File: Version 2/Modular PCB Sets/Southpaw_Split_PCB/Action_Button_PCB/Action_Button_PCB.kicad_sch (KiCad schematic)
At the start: 26 parts, among them J2 Conn_01x07_Socket, U1 Pico, X1 SW_SPST, Y1 SW_SPST

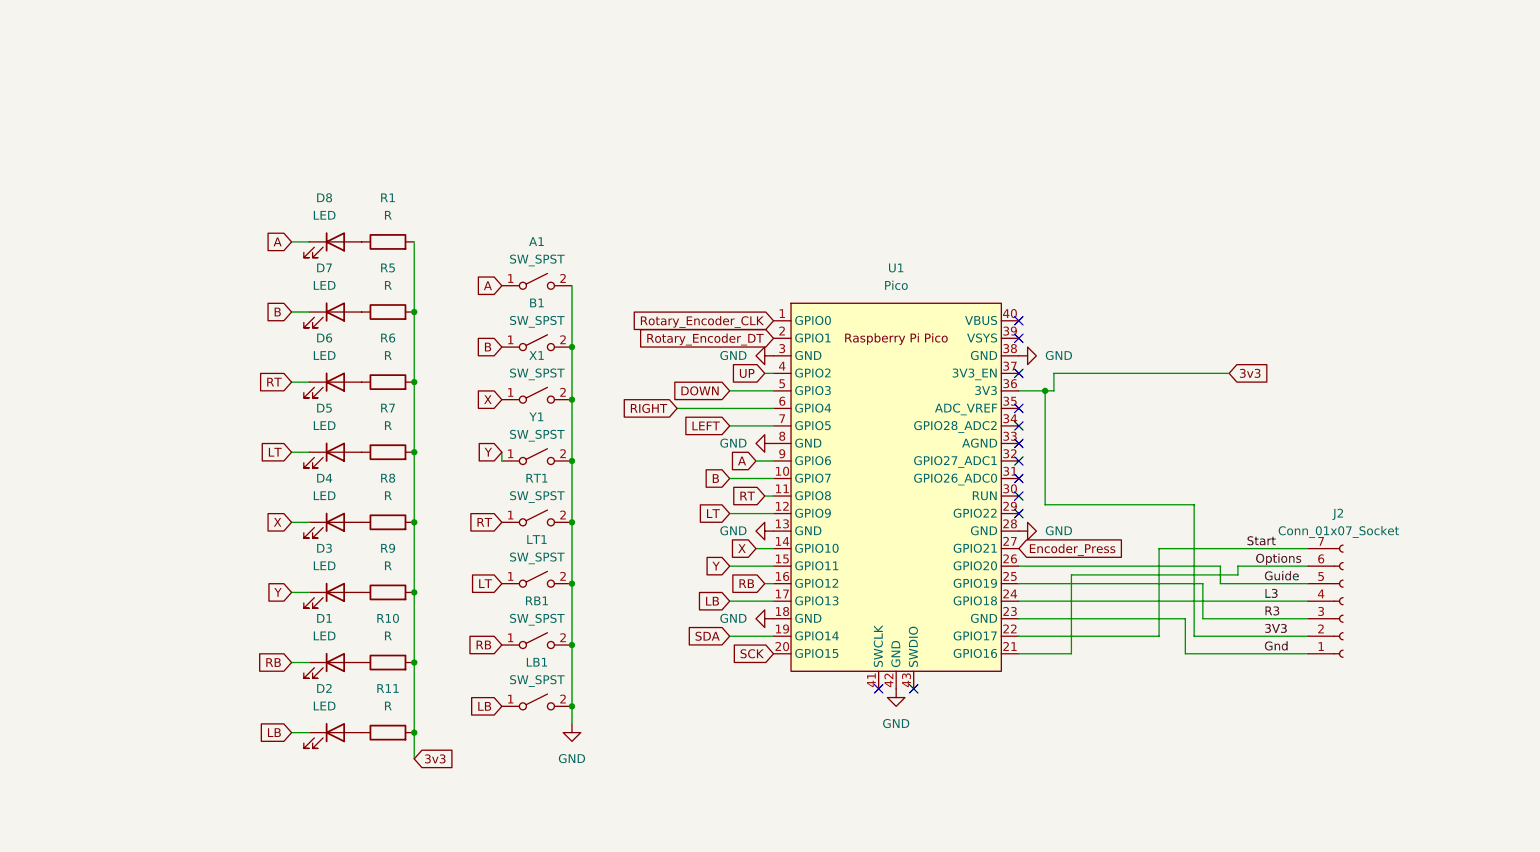
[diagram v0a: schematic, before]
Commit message: rework for schematic structure to accomodate new pico symbol and jst connectors
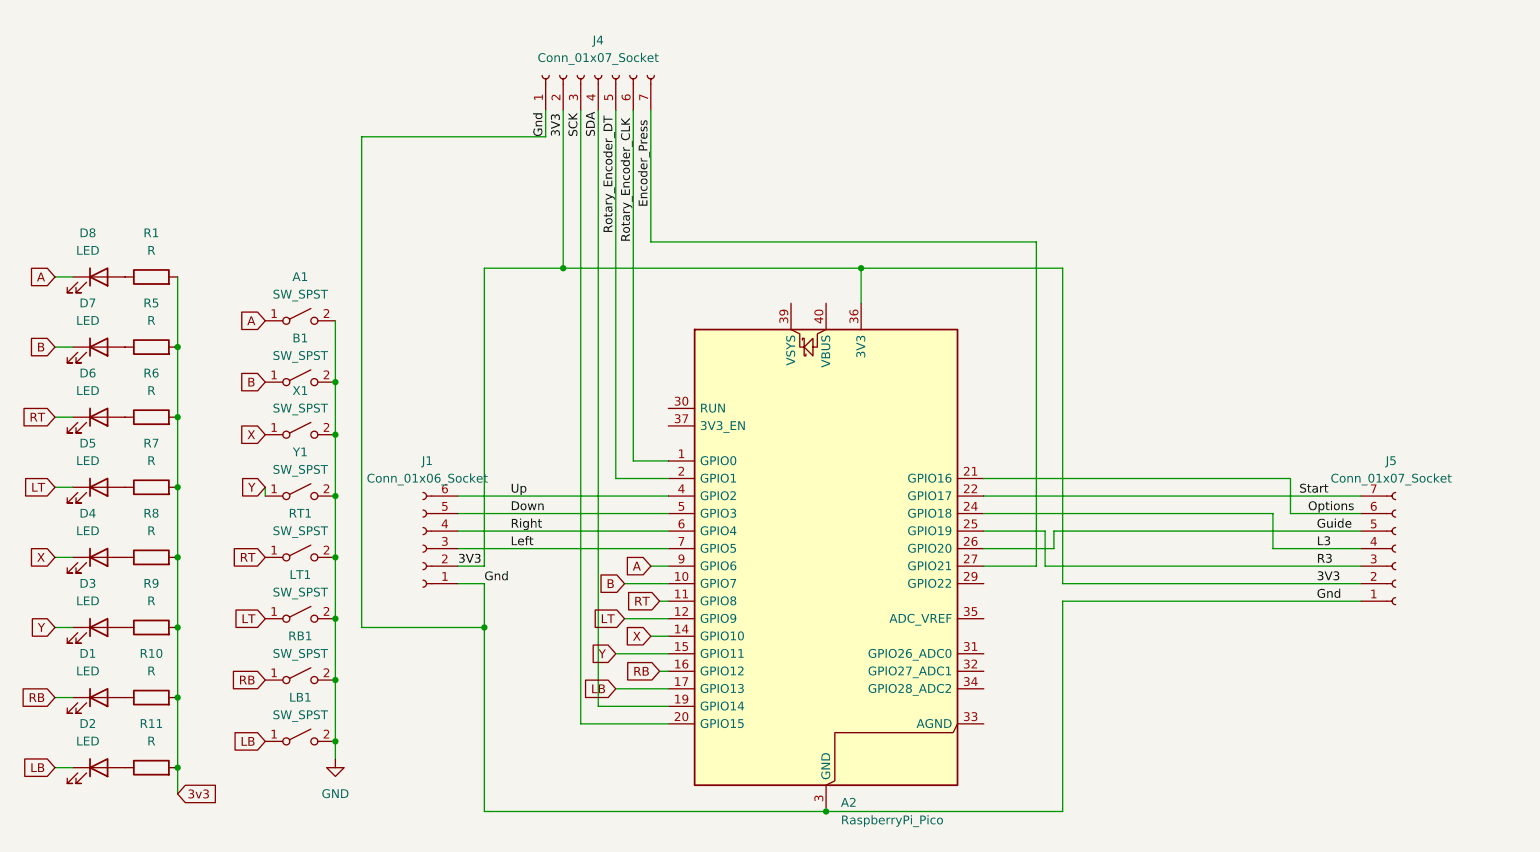
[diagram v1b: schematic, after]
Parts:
- removed J2: Conn_01x07_Socket, Connector_JST:JST_PH_B7B-PH-K_1x07_P2.00mm_Vertical, symbol Connector:Conn_01x07_Socket
- removed U1: Pico, PICO:RPi_Pico_SMD_TH, symbol pico:Pico
- added A2: RaspberryPi_Pico, Module:RaspberryPi_Pico_Common_Unspecified, symbol MCU_Module:RaspberryPi_Pico
- added J1: Conn_01x06_Socket, Connector_JST:JST_PH_B6B-PH-K_1x06_P2.00mm_Vertical, symbol Connector:Conn_01x06_Socket
- added J4, J5: Conn_01x07_Socket, Connector_JST:JST_PH_B7B-PH-K_1x07_P2.00mm_Vertical, symbol Connector:Conn_01x07_Socket
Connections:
- net A: now also A2.9 (GPIO6)
- net B: now also A2.10 (GPIO7)
- net Encoder_Press: now also A2.27 (GPIO21), J4.7 (Pin_7)
- net Gnd: now also A2.13 (GND), A2.18 (GND), A2.23 (GND), A2.28 (GND), A2.3 (GND), A2.38 (GND), A2.8 (GND), J1.1 (Pin_1), J4.1 (Pin_1), J5.1 (Pin_1)
- net Guide: now also A2.26 (GPIO20), J5.5 (Pin_5)
- net L3: now also A2.24 (GPIO18), J5.4 (Pin_4)
- net LB: now also A2.17 (GPIO13)
- net LT: now also A2.12 (GPIO9)
- net Options: now also A2.21 (GPIO16), J5.6 (Pin_6)
- net R3: now also A2.25 (GPIO19), J5.3 (Pin_3)
- net RB: now also A2.16 (GPIO12)
- net RT: now also A2.11 (GPIO8)
- net Rotary_Encoder_CLK: now also A2.1 (GPIO0), J4.6 (Pin_6)
- net Rotary_Encoder_DT: now also A2.2 (GPIO1), J4.5 (Pin_5)
- net SCK: now also A2.20 (GPIO15), J4.3 (Pin_3)
- net SDA: now also A2.19 (GPIO14), J4.4 (Pin_4)
- net Start: now also A2.22 (GPIO17), J5.7 (Pin_7)
- net X: now also A2.14 (GPIO10)
- net Y: now also A2.15 (GPIO11)
- new net 3V3: A2.36 (3V3), J1.2 (Pin_2), J4.2 (Pin_2), J5.2 (Pin_2)
- new net Down: A2.5 (GPIO3), J1.5 (Pin_5)
- new net Left: A2.7 (GPIO5), J1.3 (Pin_3)
- new net Right: A2.6 (GPIO4), J1.4 (Pin_4)
- new net Up: A2.4 (GPIO2), J1.6 (Pin_6)
- no-connect marks 12 -> 0
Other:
- moved on the sheet: A1, B1, D1, D2, D3, D4, D5, D6, D7, D8, LB1, LT1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

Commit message: created footprints for all lockout and oled display
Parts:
- renumbered D8 to D10, D7 to D11, D6 to D12, D5 to D13, D4 to D14, D3 to D15, D1 to D16, D2 to D17, J1 to J4, J4 to J5, J5 to J6, R1 to R11, R5 to R12, R6 to R13, R7 to R14, R8 to R15, R9 to R16, R10 to R17, R11 to R18

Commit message: general part layout
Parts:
- renumbered R11 to R10, R12 to R11, R13 to R12, R14 to R13, R15 to R14, R16 to R15, R17 to R16, R18 to R17
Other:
- moved on the sheet: A1, A2, B1, D10, D11, D12, D13, D14, D15, D16, D17, J4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

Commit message: First attempt to use solidworks sketches to align parts in kicad
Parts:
- renumbered D10 to D1, D11 to D2, D12 to D3, D13 to D4, D14 to D5, D15 to D6, D16 to D7, D17 to D8, J4 to J1, J5 to J2, J6 to J3, R10 to R1, R11 to R2, R12 to R3, R13 to R4, R14 to R5, R15 to R6, R16 to R7, R17 to R8
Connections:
- net 3V3 is gone; now on net 3v3: A2.36 (3V3), J1.2 (Pin_2), J2.2 (Pin_2), J3.2 (Pin_2)
- net Gnd is gone; now on net GND: A2.13 (GND), A2.18 (GND), A2.23 (GND), A2.28 (GND), A2.3 (GND), A2.38 (GND), A2.8 (GND), J1.1 (Pin_1), J2.1 (Pin_1), J3.1 (Pin_1)
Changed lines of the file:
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@@
+		)
+	)
+	(global_label "3v3"
+		(shape input)
+		(at 208.28 60.96 0)
+		(fields_autoplaced yes)
+		(effects
+			(font
+				(size 1.27 1.27)
+			)
+			(justify left)
+		)
+		(property "Intersheetrefs" "${INTERSHEET_REFS}"
+			(at 214.6518 60.96 0)
+			(effects
+				(font
+					(size 1.27 1.27)
+				)
+				(justify left)
+				(hide yes)
+			)
 		)
 	)
@@
 		(dnp no)
 		(fields_autoplaced yes)
-		(property "Reference" "J4"
+		(property "Reference" "J1"
 			(at 116.205 88.9 0)
 			(effects
@@
 		(dnp no)
 		(fields_autoplaced yes)
-		(property "Reference" "R14"
+		(property "Reference" "R5"
 			(at 76.2 96.52 90)
 			(effects
@@
 		(dnp no)
 		(fields_autoplaced yes)
-		(property "Reference" "R15"
+		(property "Reference" "R6"
 			(at 76.2 106.68 90)
 			(effects
@@
 		(dnp no)
 		(fields_autoplaced yes)
-		(property "Reference" "D15"
+		(property "Reference" "D6"
 			(at 66.9925 106.68 0)
 			(effects
@@
 		(dnp no)
 		(fields_autoplaced yes)
-		(property "Reference" "D12"
+		(property "Reference" "D3"
 			(at 66.9925 76.2 0)
 			(effects
@@
 		(dnp no)
 		(fields_autoplaced yes)
-		(property "Reference" "R13"
+		(property "Reference" "R4"
 			(at 76.2 86.36 90)
 			(effects
@@
 		(dnp no)
 		(fields_autoplaced yes)
-		(property "Reference" "D16"
+		(property "Reference" "D7"
 			(at 66.9925 116.84 0)
 			(effects
@@
 	)
 	(symbol
+		(lib_id "power:GND")
+		(at 173.99 139.7 0)
+		(unit 1)
+		(exclude_from_sim no)
+		(in_bom yes)
+		(on_board yes)
+		(dnp no)
+		(fields_autoplaced yes)
+		(property "Reference" "#PWR02"
+			(at 173.99 146.05 0)
+			(effects
+				(font
+					(size 1.27 1.27)
+				)
+				(hide yes)
+			)
+		)
+		(property "Value" "GND"
+			(at 173.99 144.78 0)
+			(effects
+				(font
+					(size 1.27 1.27)
+				)
+			)
+		)
+		(property "Footprint" ""
+			(at 173.99 139.7 0)
+			(effects
+				(font
+					(size 1.27 1.27)
+				)
+				(hide yes)
+			)
+		)
+		(property "Datasheet" ""
+			(at 173.99 139.7 0)
+			(effects
+				(font
+					(size 1.27 1.27)
+				)
+				(hide yes)
+			)
+		)
+		(property "Description" "Power symbol creates a global label with name \"GND\" , ground"
+			(at 173.99 139.7 0)
+			(effects
+				(font
+					(size 1.27 1.27)
+				)
+				(hide yes)
+			)
+		)
+		(pin "1"
+		)
+		(instances
+			(project "Action_Button_PCB"
+				(path "/a02ab618-f8ec-4fe1-96a1-02c68a63a2db"
+					(reference "#PWR02")
+					(unit 1)
+				)
+			)
+		)
+	)
+	(symbol
 		(lib_id "Switch:SW_SPST")
 		(at 97.79 77.47 0)
@@
 		(dnp no)
 		(fields_autoplaced yes)
-		(property "Reference" "D13"
+		(property "Reference" "D4"
 			(at 66.9925 86.36 0)
 			(effects
@@
 		(dnp no)
 		(fields_autoplaced yes)
-		(property "Reference" "R12"
+		(property "Reference" "R3"
 			(at 76.2 76.2 90)
 			(effects
@@
 		(dnp no)
 		(fields_autoplaced yes)
-		(property "Reference" "D17"
+		(property "Reference" "D8"
 			(at 66.9925 127 0)
 			(effects
@@
 		(dnp no)
 		(fields_autoplaced yes)
-		(property "Reference" "R16"
+		(property "Reference" "R7"
 			(at 76.2 116.84 90)
 			(effects
@@
 		(dnp no)
 		(fields_autoplaced yes)
-		(property "Reference" "J6"
+		(property "Reference" "J3"
 			(at 255.905 88.9 0)
 			(effects
@@
 		(dnp no)
 		(fields_autoplaced yes)
-		(property "Reference" "R10"
+		(property "Reference" "R1"
 			(at 76.2 55.88 90)
 			(effects
@@
 		(dnp no)
 		(fields_autoplaced yes)
-		(property "Reference" "D14"
+		(property "Reference" "D5"
 			(at 66.9925 96.52 0)
 			(effects
@@
 		(dnp no)
 		(fields_autoplaced yes)
-		(property "Reference" "R11"
+		(property "Reference" "R2"
 			(at 76.2 66.04 90)
 			(effects
@@
 		(dnp no)
 		(fields_autoplaced yes)
-		(property "Reference" "R17"
+		(property "Reference" "R8"
 			(at 76.2 127 90)
 			(effects
@@
 		(dnp no)
 		(fields_autoplaced yes)
-		(property "Reference" "D10"
+		(property "Reference" "D1"
 			(at 66.9925 55.88 0)
 			(effects
@@
 		(dnp no)
 		(fields_autoplaced yes)
-		(property "Reference" "D11"
+		(property "Reference" "D2"
 			(at 66.9925 66.04 0)
 			(effects
@@
 		(dnp no)
 		(fields_autoplaced yes)
-		(property "Reference" "J5"
+		(property "Reference" "J2"
 			(at 140.97 27.94 90)
 			(effects
